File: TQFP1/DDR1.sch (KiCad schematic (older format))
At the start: 17 parts, among them U2 MT46V32M16TG, U3 M25P32

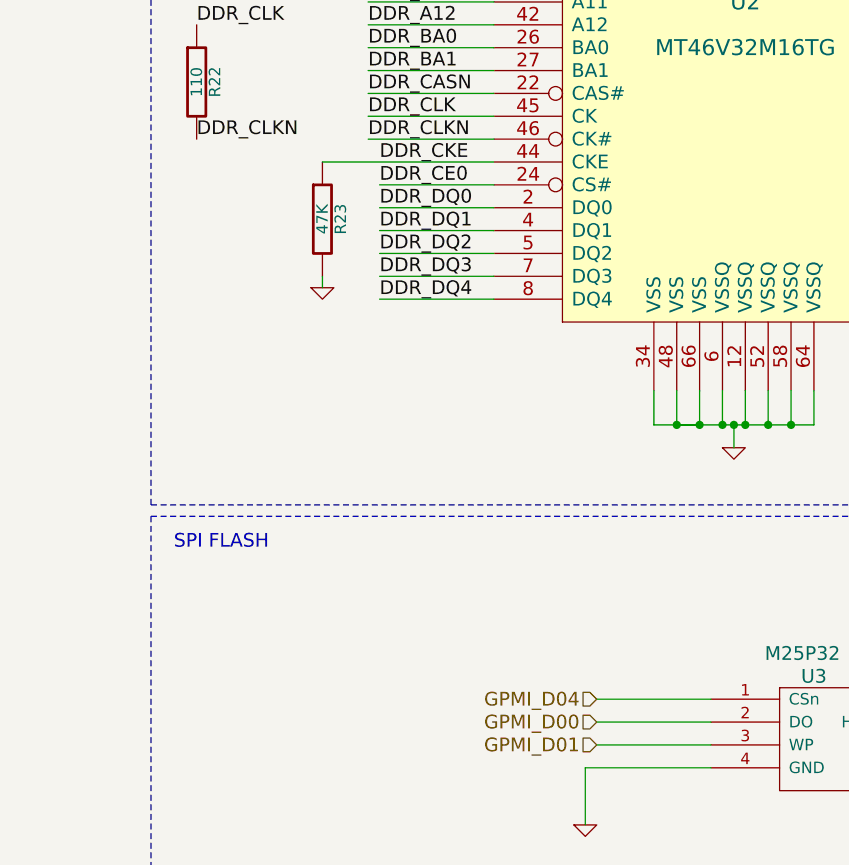
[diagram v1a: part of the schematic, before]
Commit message: Corrected PCB errors in the memory, added a MAX-232 to the UART Voltage levels and added 4 leds...
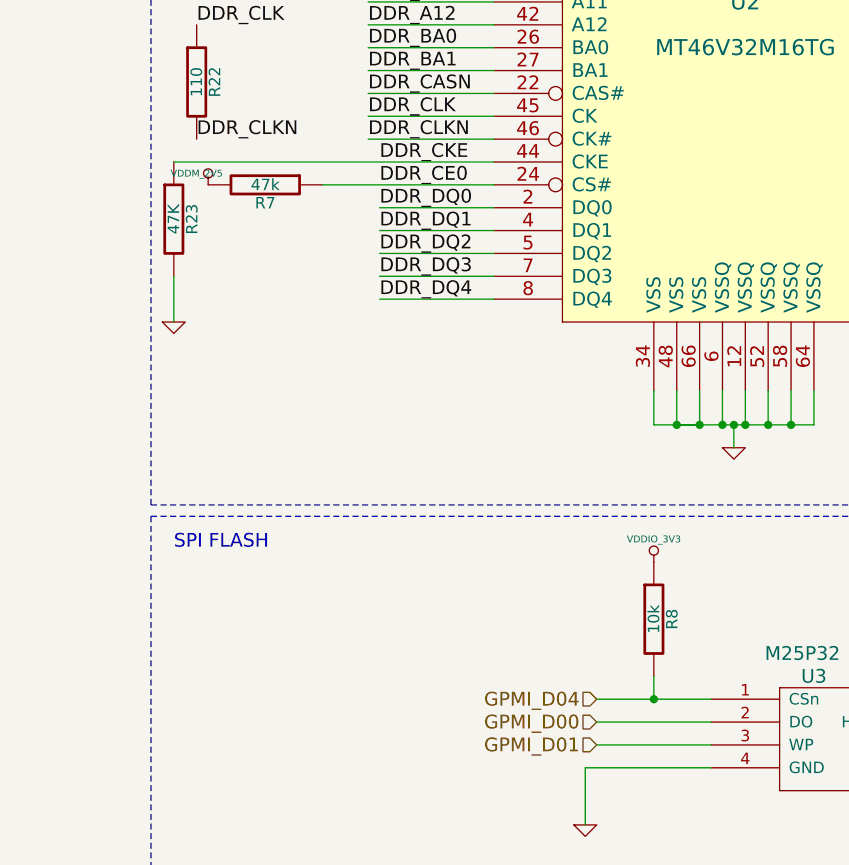
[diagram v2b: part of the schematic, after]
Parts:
- added R7: 47k, symbol R
- added R8: 10k, symbol R
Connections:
- wire segments 136 -> 137
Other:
- moved on the sheet: R23
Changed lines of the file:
@@
-EESchema Schematic File Version 2  date Wed 16 Feb 2011 10:56:53 AM COT
+EESchema Schematic File Version 2  date Tue 15 Mar 2011 01:46:05 PM COT
+LIBS:adm3101e
 LIBS:microsd
 LIBS:transistor-npn
@@
 Sheet 2 3
 Title ""
-Date "16 feb 2011"
+Date "15 mar 2011"
 Rev ""
 Comp ""
@@
 Comment4 ""
 $EndDescr
-Text Notes 5850 5500 0    60   ~ 0
-SPI FLASH
+Connection ~ 7950 6150
+Wire Wire Line
+	7950 6050 7950 6150
+Wire Wire Line
+	5850 4500 5850 4300
+Wire Wire Line
+	6500 3900 7250 3900
 Wire Notes Line
 	5750 5350 5750 7150
@@
 Wire Wire Line
 	6700 3300 7250 3300
-Wire Wire Line
-	7250 3800 6500 3800
 Connection ~ 10800 1500
 Wire Wire Line
@@
 Connection ~ 10800 2700
 Wire Wire Line
-	6500 4300 6500 4350
-Wire Wire Line
 	6700 3400 7250 3400
 Wire Wire Line
 	6700 3600 7250 3600
-Wire Wire Line
-	6750 3900 7250 3900
 Wire Wire Line
 	9450 3400 10000 3400
@@
 Wire Notes Line
 	11150 7150 5750 7150
+Wire Wire Line
+	5850 3800 7250 3800
+$Comp
+L VDDIO_3V3 #PWR01
+U 1 1 4D7E71FF
+P 7950 5550
+F 0 "#PWR01" H 7950 5650 30  0001 C CNN
+F 1 "VDDIO_3V3" H 7950 5650 30  0000 C CNN
+	1    7950 5550
+	1    0    0    -1
+$EndComp
+$Comp
+L R R8
+U 1 1 4D7E71FA
+P 7950 5800
+F 0 "R8" V 8030 5800 50  0000 C CNN
+F 1 "10k" V 7950 5800 50  0000 C CNN
+	1    7950 5800
+	1    0    0    -1
+$EndComp
+$Comp
+L VDDM_2V5 #PWR02
+U 1 1 4D7E6BF9
+P 6000 3900
+F 0 "#PWR02" H 6000 4000 30  0001 C CNN
+F 1 "VDDM_2V5" H 5950 3950 30  0000 C CNN
+	1    6000 3900
+	1    0    0    -1
+$EndComp
+$Comp
+L R R7
+U 1 1 4D7E6AED
+P 6250 3900
+F 0 "R7" V 6330 3900 50  0000 C CNN
+F 1 "47k" V 6250 3900 50  0000 C CNN
+	1    6250 3900
+	0    1    1    0
+$EndComp
+Text Notes 5850 5500 0    60   ~ 0
+SPI FLASH
 Text Notes 5850 750  0    60   ~ 0
 DDR RAM
@@
 L R R23
 U 1 1 4D418363
-P 6500 4050
-F 0 "R23" V 6580 4050 50  0000 C CNN
-F 1 "47K" V 6500 4050 50  0000 C CNN
-	1    6500 4050
-	1    0    0    -1
-$EndComp
-$Comp
-L GND #PWR01
+P 5850 4050
+F 0 "R23" V 5930 4050 50  0000 C CNN
+F 1 "47K" V 5850 4050 50  0000 C CNN
+	1    5850 4050
+	1    0    0    -1
+$EndComp
+$Comp
+L GND #PWR03
 U 1 1 4D418353
-P 6500 4350
-F 0 "#PWR01" H 6500 4350 30  0001 C CNN
-F 1 "GND" H 6500 4280 30  0001 C CNN
-	1    6500 4350
+P 5850 4500
+F 0 "#PWR03" H 5850 4500 30  0001 C CNN
+F 1 "GND" H 5850 4430 30  0001 C CNN
+	1    5850 4500
 	1    0    0    -1
 $EndComp
@@
 DDR_CKE
 $Comp
-L GND #PWR02
+L GND #PWR04
 U 1 1 4D417AF1
 P 10800 2750
-F 0 "#PWR02" H 10800 2750 30  0001 C CNN
+F 0 "#PWR04" H 10800 2750 30  0001 C CNN
 F 1 "GND" H 10800 2680 30  0001 C CNN
 	1    10800 2750
@@
 $EndComp
 $Comp
-L VDDM_2V5 #PWR03
+L VDDM_2V5 #PWR05
 U 1 1 4D417ACD
 P 10800 1450
-F 0 "#PWR03" H 10800 1550 30  0001 C CNN
+F 0 "#PWR05" H 10800 1550 30  0001 C CNN
 F 1 "VDDM_2V5" H 10800 1550 30  0000 C CNN
 	1    10800 1450
@@
 $EndComp
 $Comp
-L VDDM_2V5 #PWR04
+L VDDM_2V5 #PWR06
 U 1 1 4D4179A4
 P 7250 800
-F 0 "#PWR04" H 7250 900 30  0001 C CNN
+F 0 "#PWR06" H 7250 900 30  0001 C CNN
 F 1 "VDDM_2V5" H 7250 900 30  0000 C CNN
 	1    7250 800
@@
 $EndComp
 $Comp
-L VDDM_2V5 #PWR05
+L VDDM_2V5 #PWR07
 U 1 1 4D417999
 P 10200 800
-F 0 "#PWR05" H 10200 900 30  0001 C CNN
+F 0 "#PWR07" H 10200 900 30  0001 C CNN
 F 1 "VDDM_2V5" H 10200 900 30  0000 C CNN
 	1    10200 800
@@
 $EndComp
 $Comp
-L GND #PWR06
+L GND #PWR08
 U 1 1 4D41792B
 P 7550 1500
-F 0 "#PWR06" H 7550 1500 30  0001 C CNN
+F 0 "#PWR08" H 7550 1500 30  0001 C CNN
 F 1 "GND" H 7550 1430 30  0001 C CNN
 	1    7550 1500
@@
 $EndComp
 $Comp
-L GND #PWR07
+L GND #PWR09
 U 1 1 4D417882
 P 9600 1500
-F 0 "#PWR07" H 9600 1500 30  0001 C CNN
+F 0 "#PWR09" H 9600 1500 30  0001 C CNN
 F 1 "GND" H 9600 1430 30  0001 C CNN
 	1    9600 1500
@@
 GPMI_D04
 $Comp
-L GND #PWR08
+L GND #PWR010
 U 1 1 4D409664
 P 10400 6050
-F 0 "#PWR08" H 10400 6050 30  0001 C CNN
+F 0 "#PWR010" H 10400 6050 30  0001 C CNN
 F 1 "GND" H 10400 5980 30  0001 C CNN
 	1    10400 6050
@@
 $EndComp
 $Comp
-L VDDIO_3V3 #PWR09
+L VDDIO_3V3 #PWR011
 U 1 1 4D409635
 P 9500 5950
-F 0 "#PWR09" H 9500 6050 30  0001 C CNN
+F 0 "#PWR011" H 9500 6050 30  0001 C CNN
 F 1 "VDDIO_3V3" H 9500 6050 30  0000 C CNN
 	1    9500 5950
@@
 $EndComp
 $Comp
-L GND #PWR010
+L GND #PWR012
 U 1 1 4D409619
 P 7650 6700
-F 0 "#PWR010" H 7650 6700 30  0001 C CNN
+F 0 "#PWR012" H 7650 6700 30  0001 C CNN
 F 1 "GND" H 7650 6630 30  0001 C CNN
 	1    7650 6700
@@
 DDR_WEN
 $Comp
-L GND #PWR011
+L GND #PWR013
 U 1 1 4D319D50
 P 8300 5050
-F 0 "#PWR011" H 8300 5050 30  0001 C CNN
+F 0 "#PWR013" H 8300 5050 30  0001 C CNN
 F 1 "GND" H 8300 4980 30  0001 C CNN
 	1    8300 5050
